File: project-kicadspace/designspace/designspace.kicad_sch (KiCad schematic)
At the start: 20 parts, among them U1 ESP32-WROOM-32, U2 PCM1808PWR, U3 MAX9812, U4 TL072IDT, Y1 24.576MHz Crystal

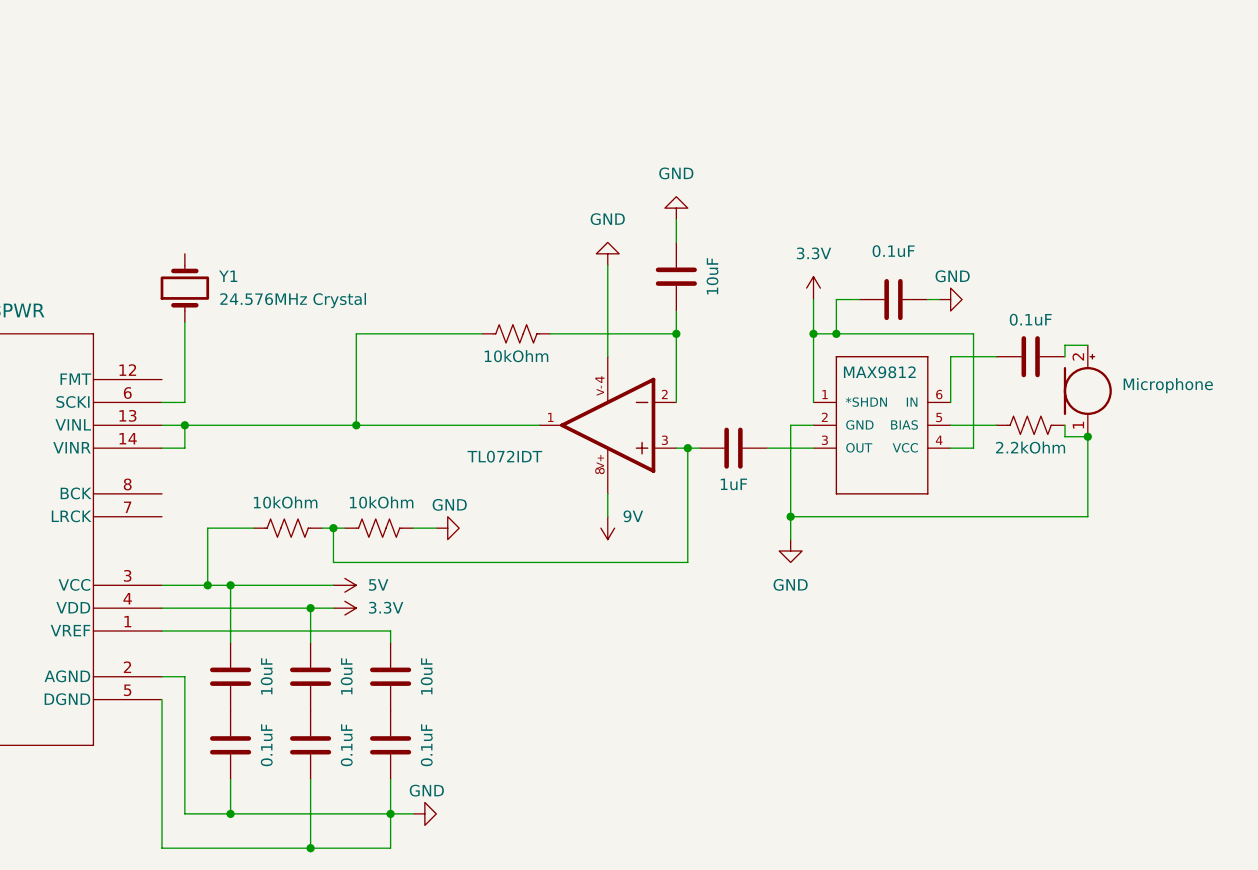
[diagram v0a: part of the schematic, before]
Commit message: feat(kicad): add resitor to stabilize 2.5V data output
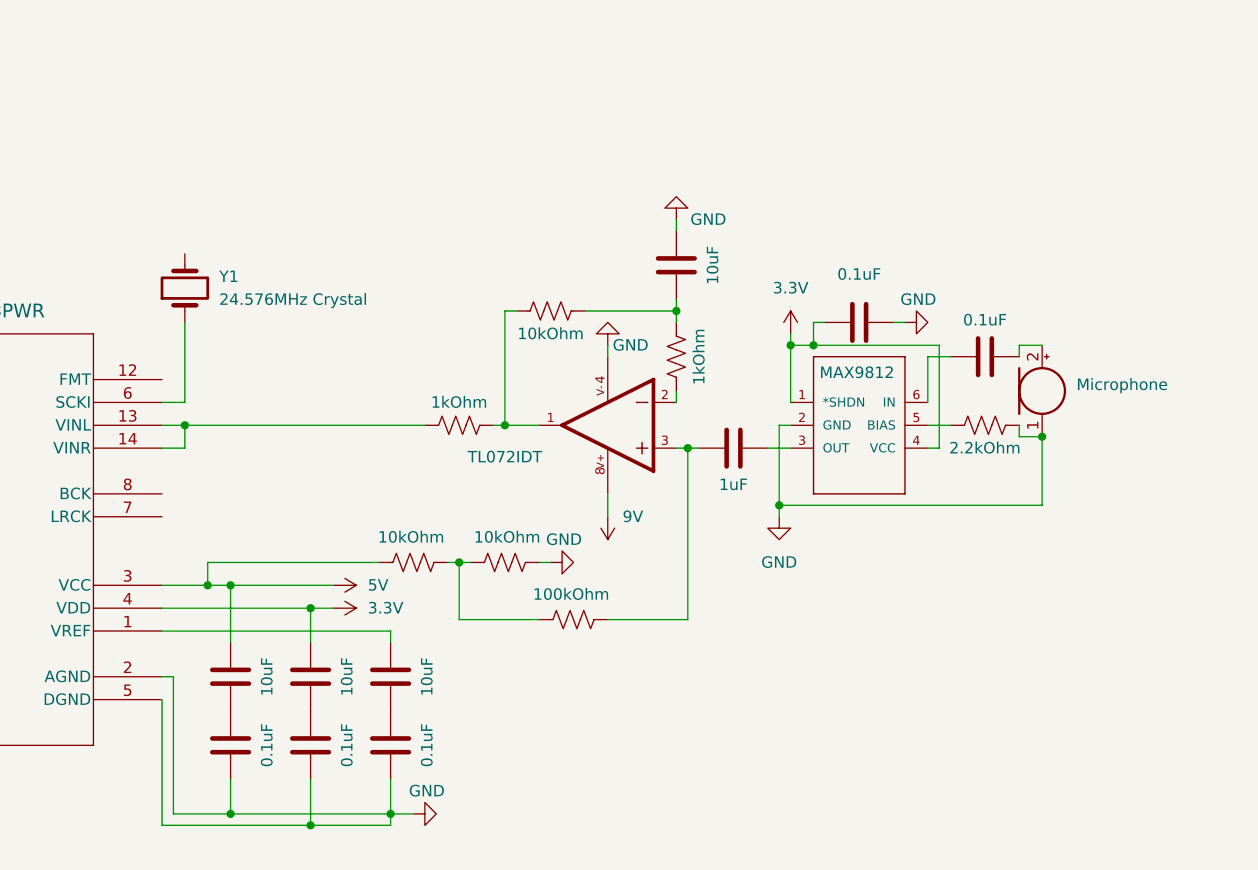
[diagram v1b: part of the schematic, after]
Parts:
- added R5, R6: 1kOhm, symbol Device:R_US
- added R7: 100kOhm, symbol Device:R_US
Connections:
- net at R2.2, R3.1: now also R7.1; no longer C3.1, U4.3
- net at R4.1, U4.1: now also R6.1; no longer U2.13 (VINL), U2.14 (VINR)
- net at C10.2, R4.2: now also R5.2; no longer U4.2
- new net: C3.1, R7.2, U4.3
- new net: R5.1, U4.2
- new net: R6.2, U2.13 (VINL), U2.14 (VINR)

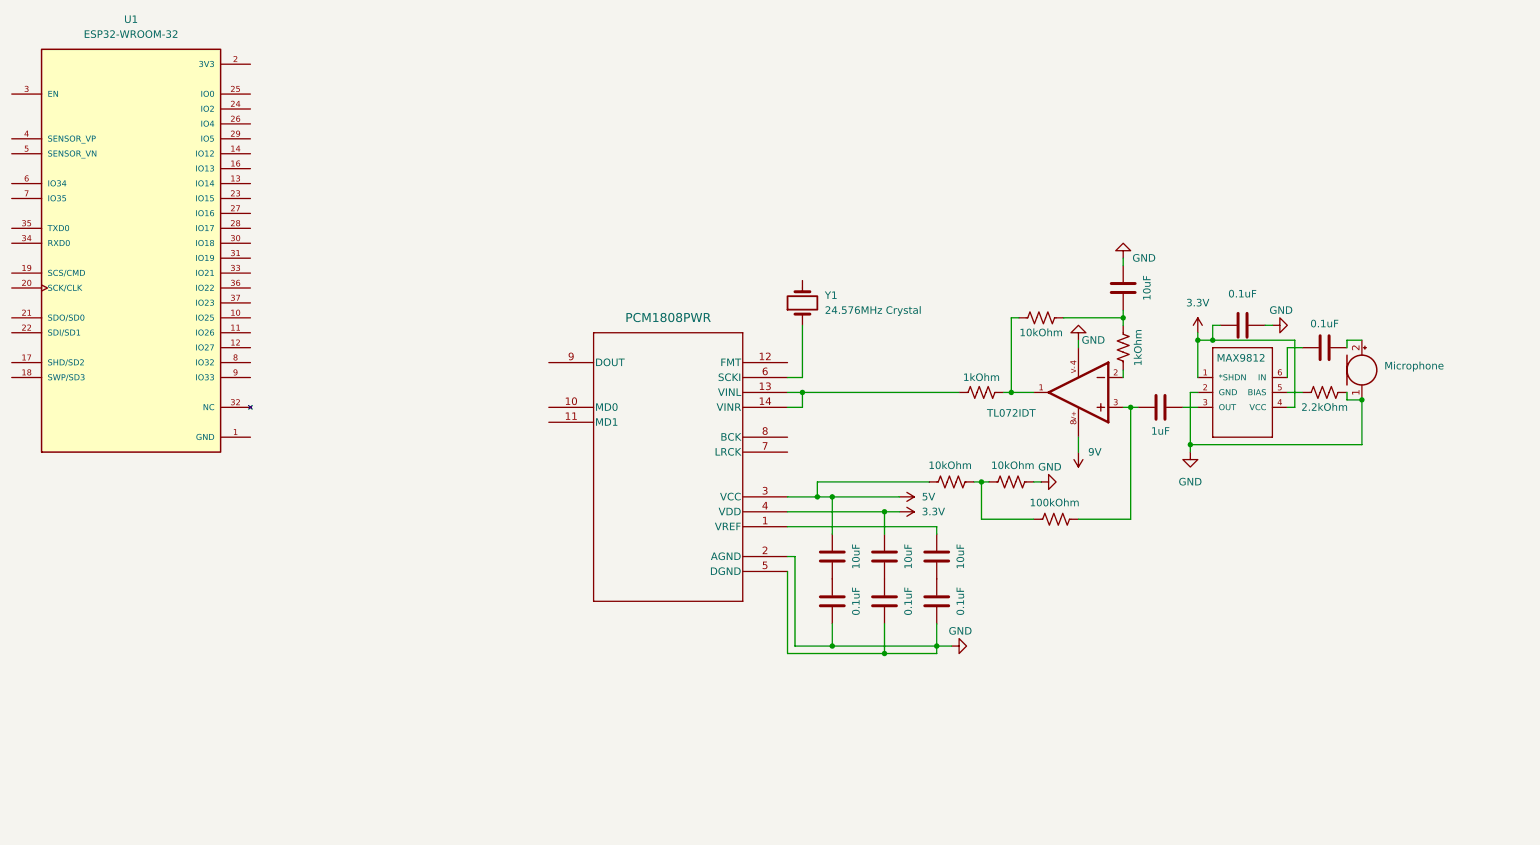
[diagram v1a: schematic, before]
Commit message: feat(kicad): finalize sch version with jb-313b & max9812
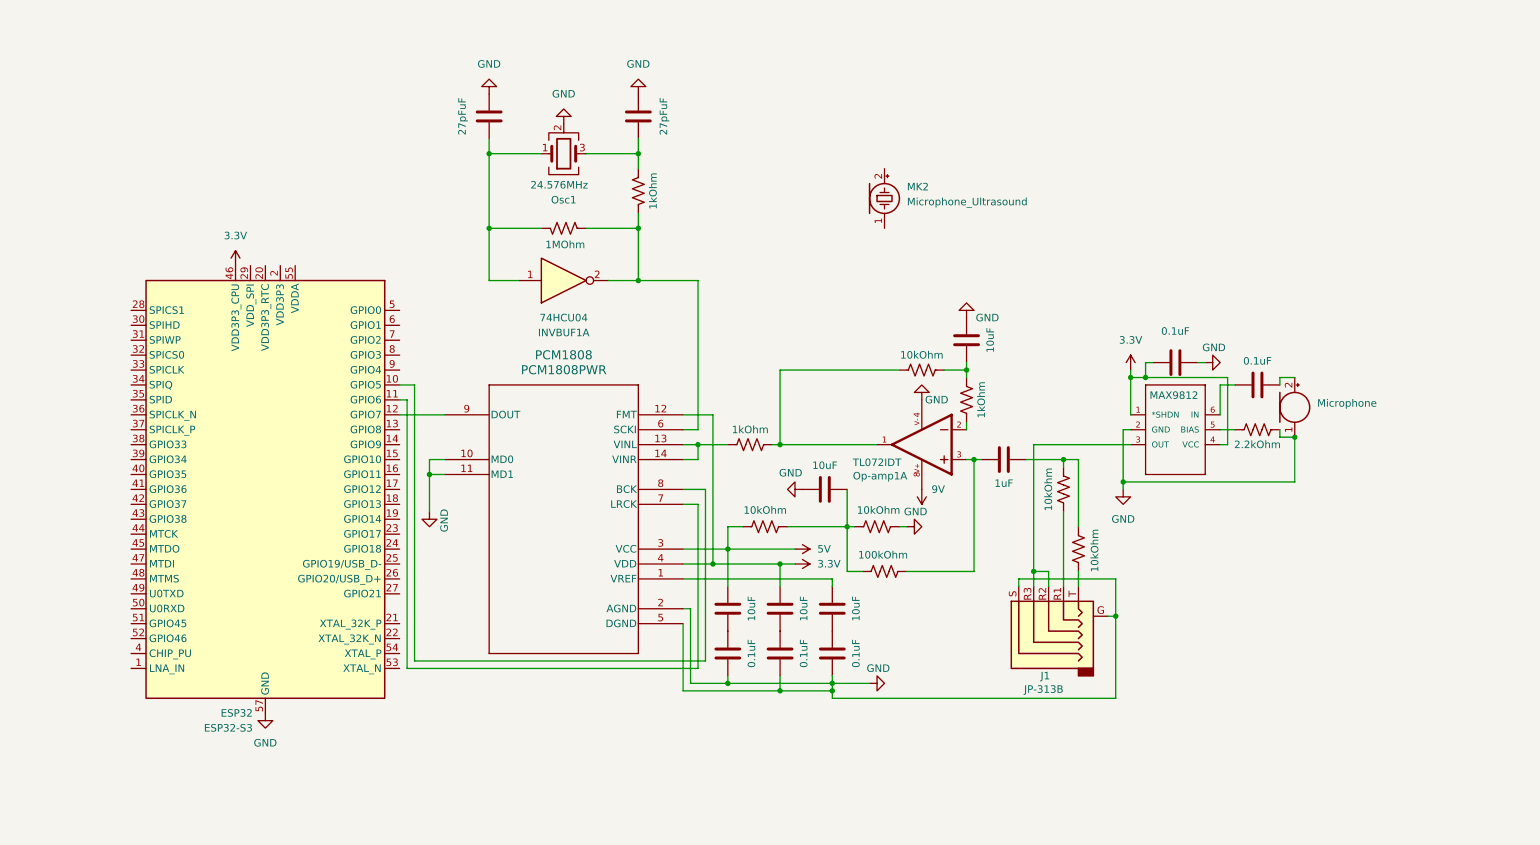
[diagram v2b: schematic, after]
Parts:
- removed U1: ESP32-WROOM-32, ESP32-WROOM-32:MODULE_ESP32-WROOM-32, symbol ESP32_WROOM_32:ESP32-WROOM-32
- removed Y1: 24.576MHz Crystal, symbol Device:Crystal
- added C11, C12: 27pFuF, symbol Device:C
- added C13: 10uF, symbol Device:C
- added ESP32: ESP32-S3, Package_DFN_QFN:QFN-56-1EP_7x7mm_P0.4mm_EP4x4mm, symbol MCU_Espressif:ESP32-S3
- added INVBUF1: 74HCU04, Package_DIP:DIP-14_W7.62mm_Socket, symbol 74xx:74HC04
- added J1: JP-313B, Connector_Audio:Jack_3.5mm_PJ311_Horizontal, symbol Connector_Audio:AudioJack5_Ground
- added MK2: Microphone_Ultrasound, symbol Device:Microphone_Ultrasound
- added Osc1: 24.576MHz, Crystal:Crystal_SMD_7050-4Pin_7.0x5.0mm, symbol Device:Crystal_GND24
- added R10, R11: 10kOhm, symbol Device:R_US
- added R8: 1MOhm, symbol Device:R_US
- added R9: 1kOhm, symbol Device:R_US
- renumbered U4 to Op-amp1, U2 to PCM1808
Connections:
- net 3.3V: now also PCM1808.12 (FMT), ESP32.46 (VDD3P3_CPU)
- net GND: now also PCM1808.10 (MD0), PCM1808.11 (MD1), C11.2, C12.2, C13.1, ESP32.57 (GND), J1.G, J1.S, Osc1.2 (G), Osc1.4 (G)
- net at U3.3 (OUT): now also J1.R2, J1.R3; no longer C3.2
- net at R2.2, R3.1, R7.1: now also C13.2
- net at PCM1808.6 (SCKI): now also INVBUF1.2, R8.2, R9.2
- net at PCM1808.7 (LRCK): now also ESP32.11 (GPIO6)
- net at PCM1808.8 (BCK): now also ESP32.10 (GPIO5)
- net at PCM1808.9 (DOUT): now also ESP32.12 (GPIO7)
- new net: ESP32.2 (VDD3P3), ESP32.3 (VDD3P3)
- new net: ESP32.55 (VDDA), ESP32.56 (VDDA)
- new net: C3.2, R10.1, R11.1
- new net: J1.T, R10.2
- new net: C11.1, INVBUF1.1, Osc1.1, R8.1
- new net: C12.1, Osc1.3, R9.1
- new net: J1.R1, R11.2

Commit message: feat(sch): add TCT40-16R support line & redirect signal line to PCM1808
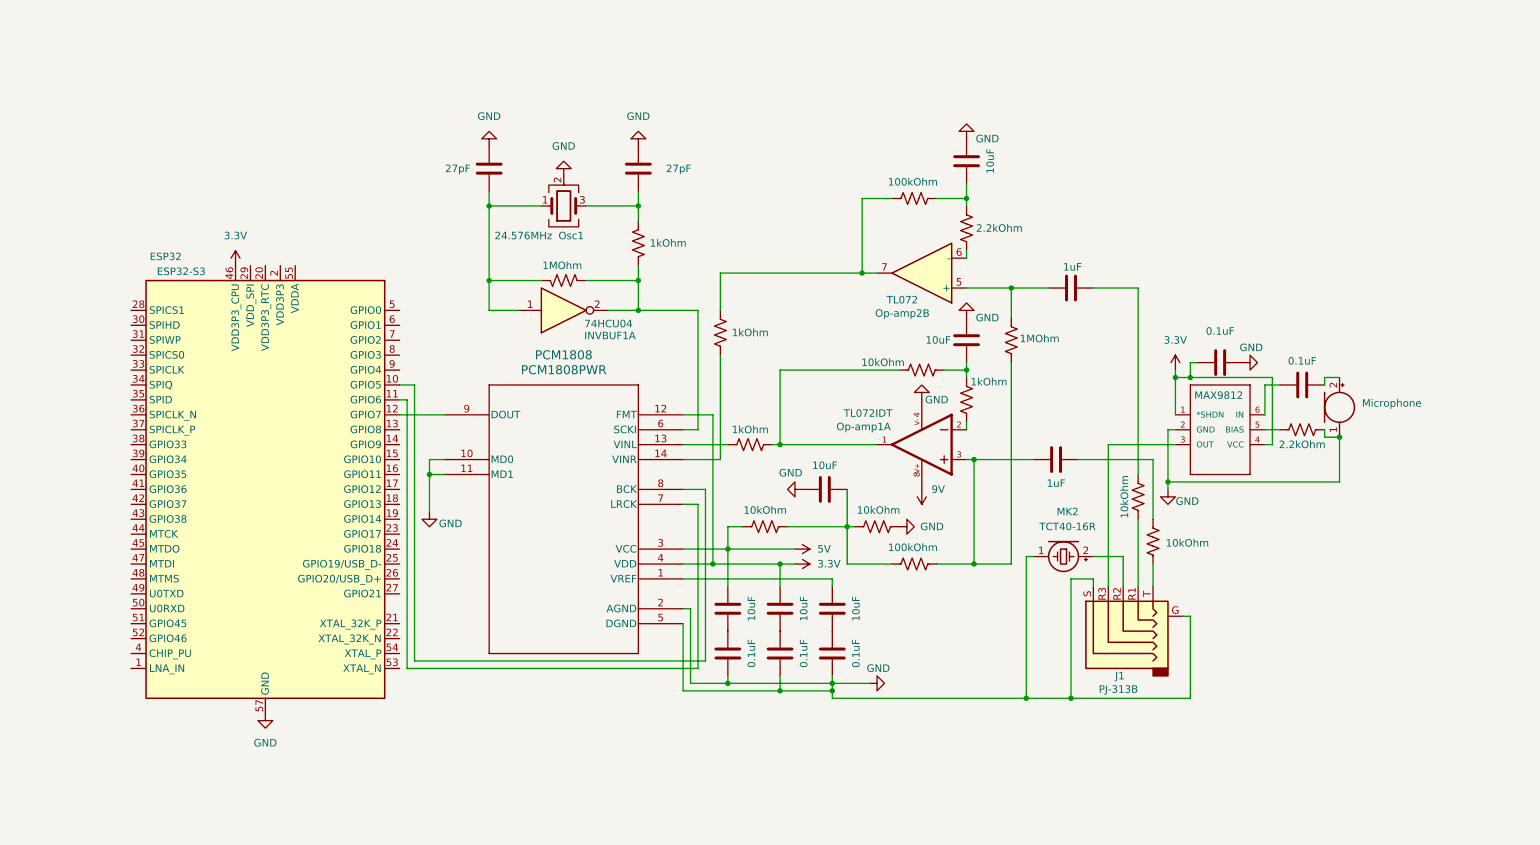
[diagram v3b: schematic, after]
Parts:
- added C14: 10uF, symbol Device:C
- added C15: 1uF, symbol Device:C
- added Op-amp2: TL072, symbol Amplifier_Operational:TL072
- added R12: 1MOhm, symbol Device:R_US
- added R13: 100kOhm, symbol Device:R_US
- added R14: 2.2kOhm, symbol Device:R_US
- added R15: 1kOhm, symbol Device:R_US
- C11, C12: value 27pFuF -> 27pF
- J1: value JP-313B -> PJ-313B
- MK2: value Microphone_Ultrasound -> TCT40-16R
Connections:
- net GND: now also MK2.1 (-), C14.1
- net at J1.R3, U3.3 (OUT): no longer J1.R2
- net at C3.1, Op-amp1.3, R7.2: now also R12.2
- net at MK2.2 (+): now also J1.R2
- net at C3.2, R10.1: no longer R11.1
- net at PCM1808.13 (VINL), R6.2: no longer PCM1808.14 (VINR)
- new net: C15.1, Op-amp2.5 (+), R12.1
- new net: C15.2, R11.1
- new net: C14.2, R13.2, R14.2
- new net: Op-amp2.6 (-), R14.1
- new net: Op-amp2.7, R13.1, R15.2
- new net: PCM1808.14 (VINR), R15.1
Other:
- moved on the sheet: INVBUF1A, J1, MK2, Osc1

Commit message: feat(sch): split sch into hier-sch to simplified sch
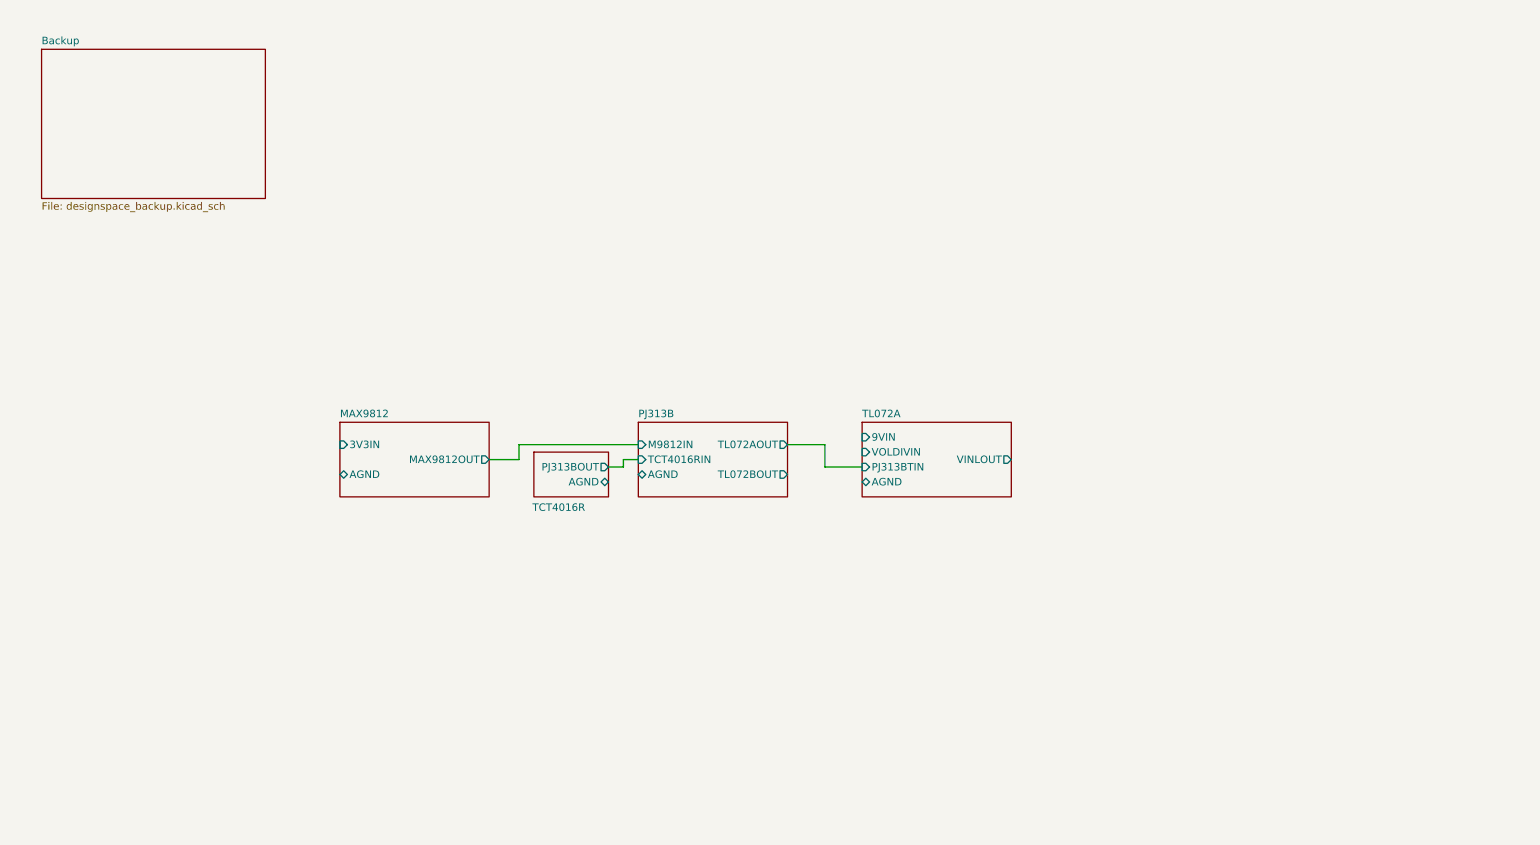
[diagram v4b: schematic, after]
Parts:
- removed C1, C2, C5, C7, C9: 0.1uF, symbol Device:C
- removed C10, C13, C14, C4, C6, C8: 10uF, symbol Device:C
- removed C11, C12: 27pF, symbol Device:C
- removed C15, C3: 1uF, symbol Device:C
- removed ESP32: ESP32-S3, Package_DFN_QFN:QFN-56-1EP_7x7mm_P0.4mm_EP4x4mm, symbol MCU_Espressif:ESP32-S3
- removed INVBUF1: 74HCU04, Package_DIP:DIP-14_W7.62mm_Socket, symbol 74xx:74HC04
- removed J1: PJ-313B, Connector_Audio:Jack_3.5mm_PJ311_Horizontal, symbol Connector_Audio:AudioJack5_Ground
- removed MK1: Microphone, symbol Device:Microphone
- removed MK2: TCT40-16R, symbol Device:Microphone_Ultrasound
- removed Op-amp1: TL072IDT, TL072IDT:SOIC127P600X175-8N, symbol TL072IDT:TL072IDT
- removed Op-amp2: TL072, symbol Amplifier_Operational:TL072
- removed Osc1: 24.576MHz, Crystal:Crystal_SMD_7050-4Pin_7.0x5.0mm, symbol Device:Crystal_GND24
- removed PCM1808: PCM1808PWR, PW14, symbol PCM1808:PCM1808PWR
- removed R1, R14: 2.2kOhm, symbol Device:R_US
- removed R10, R11, R2, R3, R4: 10kOhm, symbol Device:R_US
- removed R12, R8: 1MOhm, symbol Device:R_US
- removed R13, R7: 100kOhm, symbol Device:R_US
- removed R15, R5, R6, R9: 1kOhm, symbol Device:R_US
- removed U3: MAX9812, MAX9812LEXTT:21-0077G, symbol MAX9812:MAX9812
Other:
- added sheet Backup (designspace_backup.kicad_sch)
- added sheet MAX9812 (designspace_max9812.kicad_sch)
- added sheet PJ313B (designspace_pj313b.kicad_sch)
- added sheet TCT4016R (designspace_tct4016r.kicad_sch)
- added sheet TL072A (designspace_tl072a.kicad_sch)
